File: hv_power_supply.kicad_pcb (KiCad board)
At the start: 2 copper layers, 49.5 x 44.5 mm, 19 parts, among them P1 CONN_01X09, Q1 IRF644PBF, U1 MAX1771, U2 MCP41050

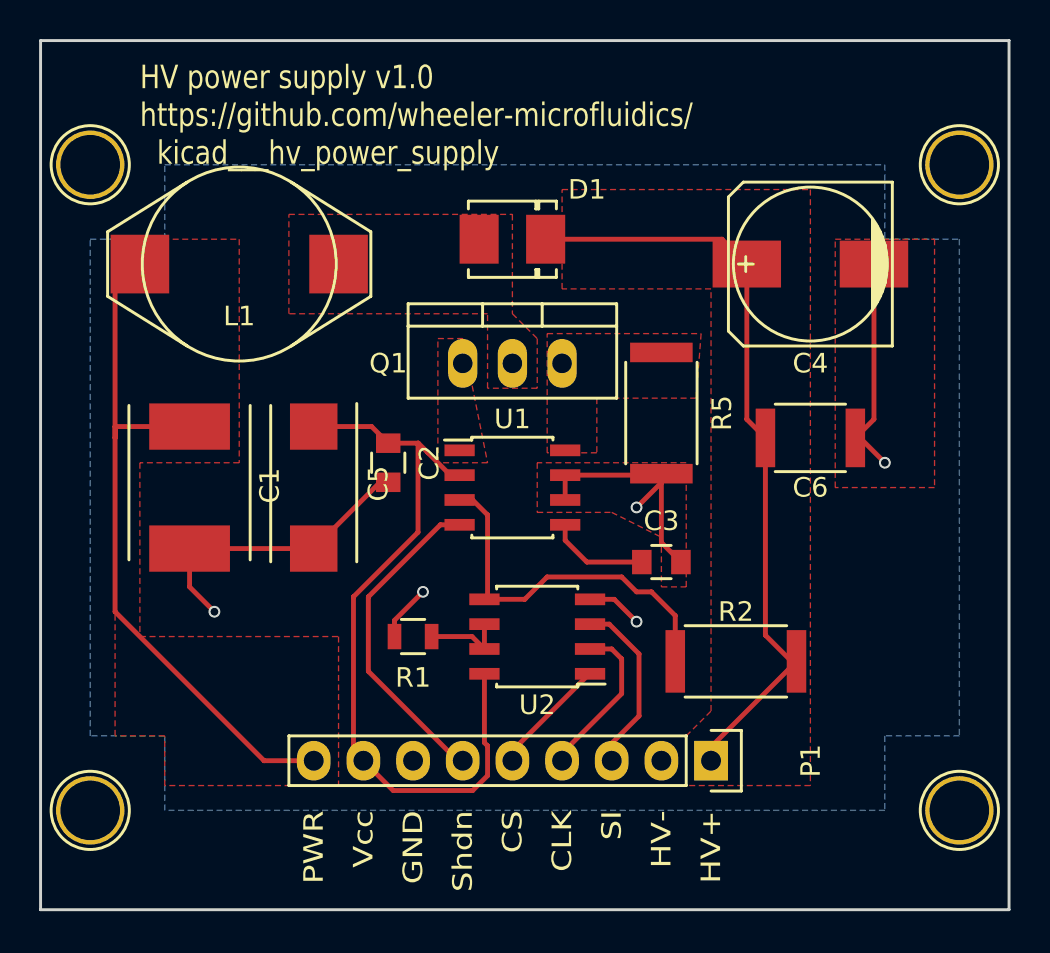
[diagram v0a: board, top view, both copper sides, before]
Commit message: Add extra via holes to connect back side of single-sided board
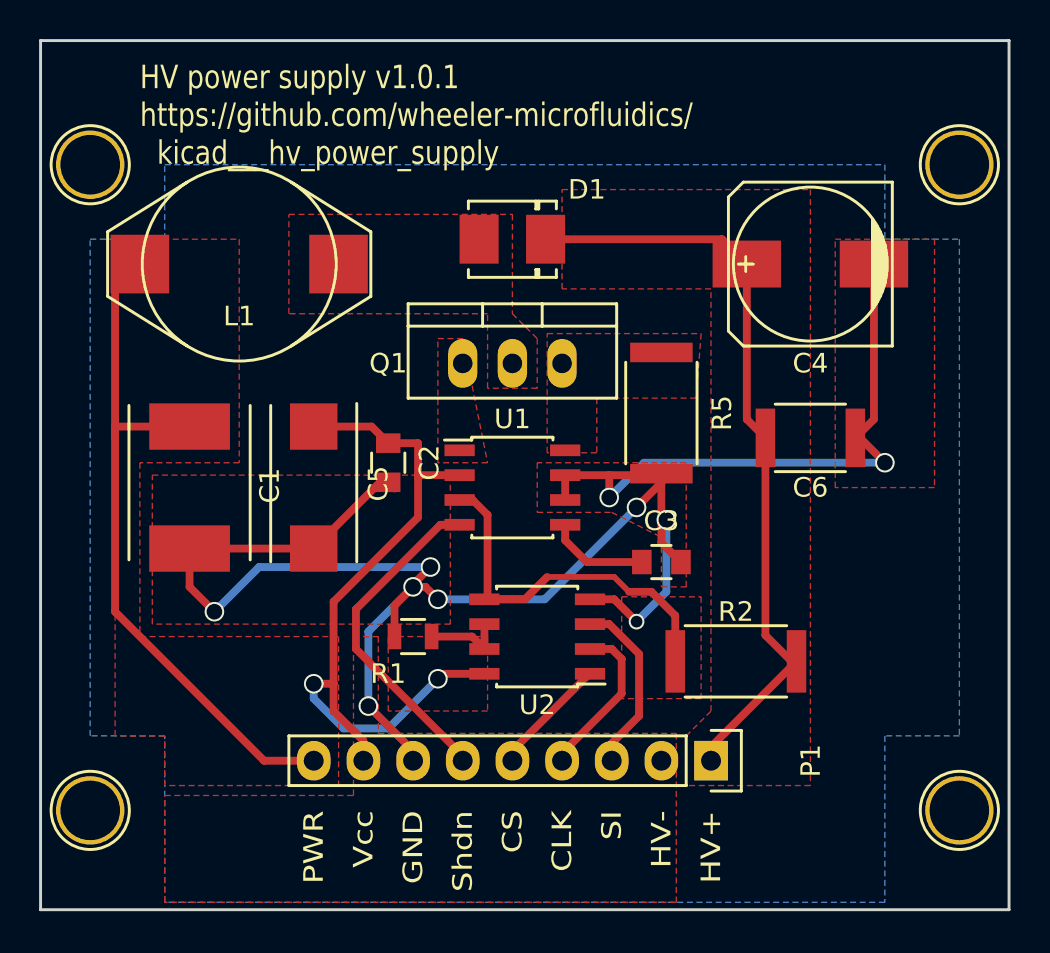
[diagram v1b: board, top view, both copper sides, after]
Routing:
- net DGND: track 46.7 -> 106.6 mm, vias 5 -> 10
- net VCC: track 38.9 -> 40.9 mm, vias 0 -> 2
- net SHDN: track 16.9 -> 17.7 mm
- added copper zone on F.Cu, net VCC
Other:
- net class Default: clearance 0.25 -> 0.4; trace_width 0.25 -> 0.4; via_dia 0.6 -> 1; via_drill 0.4 -> 0.8
- rule trace_clearance: 0.25 -> 0.4
- board text added: "HV power supply v1.0.1 https://github.com/wheeler-microfluidics/ kicad___hv_power_supply"
- board text removed: "HV power supply v1.0 https://github.com/wheeler-microfluidics/ kicad___hv_power_supply"
